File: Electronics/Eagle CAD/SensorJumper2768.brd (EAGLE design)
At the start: 9.1 x 6.3 mm, 1 part, among them J1 CONN-14-1.27X2

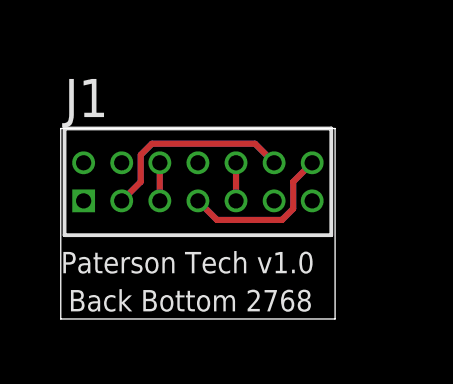
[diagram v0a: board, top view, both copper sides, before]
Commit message: Adjust certain holes sizes in PCB designs
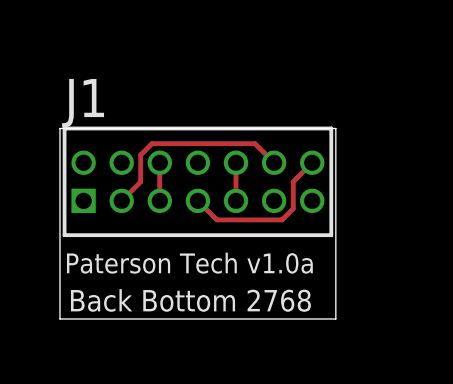
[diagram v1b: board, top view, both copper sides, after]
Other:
- board size 9.1 x 6.3 mm -> 9.2 x 6.3 mm
- board text added: "Paterson Tech v1.0a"
- board text removed: "Paterson Tech v1.0"
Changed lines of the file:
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@@
 <layers>
 <layer number="1" name="Top" color="4" fill="1" visible="no" active="yes"/>
+<layer number="2" name="Route2" color="1" fill="3" visible="no" active="no"/>
+<layer number="3" name="Route3" color="4" fill="3" visible="no" active="no"/>
+<layer number="4" name="Route4" color="1" fill="4" visible="no" active="no"/>
+<layer number="5" name="Route5" color="4" fill="4" visible="no" active="no"/>
+<layer number="6" name="Route6" color="1" fill="8" visible="no" active="no"/>
+<layer number="7" name="Route7" color="4" fill="8" visible="no" active="no"/>
+<layer number="8" name="Route8" color="1" fill="2" visible="no" active="no"/>
+<layer number="9" name="Route9" color="4" fill="2" visible="no" active="no"/>
+<layer number="10" name="Route10" color="1" fill="7" visible="no" active="no"/>
+<layer number="11" name="Route11" color="4" fill="7" visible="no" active="no"/>
+<layer number="12" name="Route12" color="1" fill="5" visible="no" active="no"/>
+<layer number="13" name="Route13" color="4" fill="5" visible="no" active="no"/>
+<layer number="14" name="Route14" color="1" fill="6" visible="no" active="no"/>
+<layer number="15" name="Route15" color="4" fill="6" visible="no" active="no"/>
 <layer number="16" name="Bottom" color="1" fill="1" visible="yes" active="yes"/>
 <layer number="17" name="Pads" color="2" fill="1" visible="yes" active="yes"/>
@@
 <board>
 <plain>
-<wire x1="0" y1="0" x2="9.144" y2="0" width="0" layer="20"/>
-<wire x1="9.144" y1="0" x2="9.144" y2="6.35" width="0" layer="20"/>
-<wire x1="9.144" y1="6.35" x2="0" y2="6.35" width="0" layer="20"/>
-<wire x1="0" y1="6.35" x2="0" y2="0" width="0" layer="20"/>
+<wire x1="-0.0254" y1="0" x2="9.1694" y2="0" width="0" layer="20"/>
+<wire x1="9.1694" y1="0" x2="9.1694" y2="6.35" width="0" layer="20"/>
+<wire x1="9.1694" y1="6.35" x2="-0.0254" y2="6.35" width="0" layer="20"/>
+<wire x1="-0.0254" y1="6.35" x2="-0.0254" y2="0" width="0" layer="20"/>
 <text x="0.254" y="0.254" size="0.7112" layer="21">Back Bottom 2768</text>
-<text x="0" y="1.524" size="0.7112" layer="21">Paterson Tech v1.0</text>
-<text x="9.017" y="1.524" size="0.7112" layer="22" rot="MR0">Paterson Tech v1.0</text>
-<text x="9.017" y="0.381" size="0.7112" layer="22" rot="MR0">Panel Bottom 2768</text>
+<text x="0.127" y="1.524" size="0.6604" layer="21">Paterson Tech v1.0a</text>
+<text x="9.017" y="1.524" size="0.6604" layer="22" rot="MR0">Paterson Tech v1.0a</text>
+<text x="9.017" y="0.381" size="0.6858" layer="22" rot="MR0">Panel Bottom 2768</text>
 </plain>
 <attributes>
@@
 <contactref element="J1" pad="3"/>
 <contactref element="J1" pad="12"/>
-<wire x1="2.667" y1="5.47003125" x2="3.03896875" y2="5.842" width="0.2032" layer="1" grouprefs="CONNECTOR"/>
-<wire x1="2.032" y1="3.937" x2="2.667" y2="4.572" width="0.2032" layer="1" grouprefs="CONNECTOR"/>
-<wire x1="2.667" y1="4.572" x2="2.667" y2="5.47003125" width="0.2032" layer="1" grouprefs="CONNECTOR"/>
-<wire x1="6.477" y1="5.842" x2="7.112" y2="5.207" width="0.2032" layer="1" grouprefs="CONNECTOR"/>
-<wire x1="3.03896875" y1="5.842" x2="6.477" y2="5.842" width="0.2032" layer="1" grouprefs="CONNECTOR"/>
-<wire x1="2.667" y1="5.47003125" x2="3.03896875" y2="5.842" width="0.2032" layer="16"/>
-<wire x1="2.032" y1="3.937" x2="2.667" y2="4.572" width="0.2032" layer="16"/>
-<wire x1="2.667" y1="4.572" x2="2.667" y2="5.47003125" width="0.2032" layer="16"/>
-<wire x1="6.477" y1="5.842" x2="7.112" y2="5.207" width="0.2032" layer="16"/>
-<wire x1="3.03896875" y1="5.842" x2="6.477" y2="5.842" width="0.2032" layer="16"/>
+<wire x1="2.667" y1="5.47003125" x2="3.03896875" y2="5.842" width="0.1524" layer="1" grouprefs="CONNECTOR"/>
+<wire x1="2.032" y1="3.937" x2="2.667" y2="4.572" width="0.1524" layer="1" grouprefs="CONNECTOR"/>
+<wire x1="2.667" y1="4.572" x2="2.667" y2="5.47003125" width="0.1524" layer="1" grouprefs="CONNECTOR"/>
+<wire x1="6.477" y1="5.842" x2="7.112" y2="5.207" width="0.1524" layer="1" grouprefs="CONNECTOR"/>
+<wire x1="3.03896875" y1="5.842" x2="6.477" y2="5.842" width="0.1524" layer="1" grouprefs="CONNECTOR"/>
+<wire x1="2.667" y1="5.47003125" x2="3.03896875" y2="5.842" width="0.1524" layer="16"/>
+<wire x1="2.032" y1="3.937" x2="2.667" y2="4.572" width="0.1524" layer="16"/>
+<wire x1="2.667" y1="4.572" x2="2.667" y2="5.47003125" width="0.1524" layer="16"/>
+<wire x1="6.477" y1="5.842" x2="7.112" y2="5.207" width="0.1524" layer="16"/>
+<wire x1="3.03896875" y1="5.842" x2="6.477" y2="5.842" width="0.1524" layer="16"/>
 </signal>
 <signal name="N$2">
 <contactref element="J1" pad="7"/>
 <contactref element="J1" pad="14"/>
-<wire x1="7.747" y1="3.67396875" x2="7.37503125" y2="3.302" width="0.2032" layer="1" grouprefs="CONNECTOR"/>
-<wire x1="8.382" y1="5.207" x2="7.747" y2="4.572" width="0.2032" layer="1" grouprefs="CONNECTOR"/>
-<wire x1="7.747" y1="4.572" x2="7.747" y2="3.67396875" width="0.2032" layer="1" grouprefs="CONNECTOR"/>
-<wire x1="5.207" y1="3.302" x2="4.572" y2="3.937" width="0.2032" layer="1" grouprefs="CONNECTOR"/>
-<wire x1="7.37503125" y1="3.302" x2="5.207" y2="3.302" width="0.2032" layer="1" grouprefs="CONNECTOR"/>
-<wire x1="4.572" y1="3.937" x2="5.207" y2="3.302" width="0.2032" layer="16"/>
-<wire x1="7.37503125" y1="3.302" x2="7.747" y2="3.67396875" width="0.2032" layer="16"/>
-<wire x1="7.747" y1="4.572" x2="8.382" y2="5.207" width="0.2032" layer="16"/>
-<wire x1="5.207" y1="3.302" x2="7.37503125" y2="3.302" width="0.2032" layer="16"/>
-<wire x1="7.747" y1="3.67396875" x2="7.747" y2="4.572" width="0.2032" layer="16"/>
+<wire x1="7.747" y1="3.67396875" x2="7.37503125" y2="3.302" width="0.1524" layer="1" grouprefs="CONNECTOR"/>
+<wire x1="8.382" y1="5.207" x2="7.747" y2="4.572" width="0.1524" layer="1" grouprefs="CONNECTOR"/>
+<wire x1="7.747" y1="4.572" x2="7.747" y2="3.67396875" width="0.1524" layer="1" grouprefs="CONNECTOR"/>
+<wire x1="5.207" y1="3.302" x2="4.572" y2="3.937" width="0.1524" layer="1" grouprefs="CONNECTOR"/>
+<wire x1="7.37503125" y1="3.302" x2="5.207" y2="3.302" width="0.1524" layer="1" grouprefs="CONNECTOR"/>
+<wire x1="4.572" y1="3.937" x2="5.207" y2="3.302" width="0.1524" layer="16"/>
+<wire x1="7.37503125" y1="3.302" x2="7.747" y2="3.67396875" width="0.1524" layer="16"/>
+<wire x1="7.747" y1="4.572" x2="8.382" y2="5.207" width="0.1524" layer="16"/>
+<wire x1="5.207" y1="3.302" x2="7.37503125" y2="3.302" width="0.1524" layer="16"/>
+<wire x1="7.747" y1="3.67396875" x2="7.747" y2="4.572" width="0.1524" layer="16"/>
 </signal>
 <signal name="N$3">
 <contactref element="J1" pad="9"/>
 <contactref element="J1" pad="10"/>
-<wire x1="5.842" y1="5.207" x2="5.842" y2="3.937" width="0.2032" layer="1" grouprefs="CONNECTOR"/>
-<wire x1="5.842" y1="5.207" x2="5.842" y2="3.937" width="0.2032" layer="16"/>
+<wire x1="5.842" y1="5.207" x2="5.842" y2="3.937" width="0.1524" layer="1" grouprefs="CONNECTOR"/>
+<wire x1="5.842" y1="5.207" x2="5.842" y2="3.937" width="0.1524" layer="16"/>
 </signal>
 <signal name="N$4">
 <contactref element="J1" pad="5"/>
 <contactref element="J1" pad="6"/>
-<wire x1="3.302" y1="5.207" x2="3.302" y2="3.937" width="0.2032" layer="1" grouprefs="CONNECTOR"/>
-<wire x1="3.302" y1="3.937" x2="3.302" y2="5.207" width="0.2032" layer="16"/>
+<wire x1="3.302" y1="5.207" x2="3.302" y2="3.937" width="0.1524" layer="1" grouprefs="CONNECTOR"/>
+<wire x1="3.302" y1="3.937" x2="3.302" y2="5.207" width="0.1524" layer="16"/>
 </signal>
 </signals>
